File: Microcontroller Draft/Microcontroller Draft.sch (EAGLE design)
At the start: 18 parts, among them IC1 74LS251N, IC2 PIC16F628P

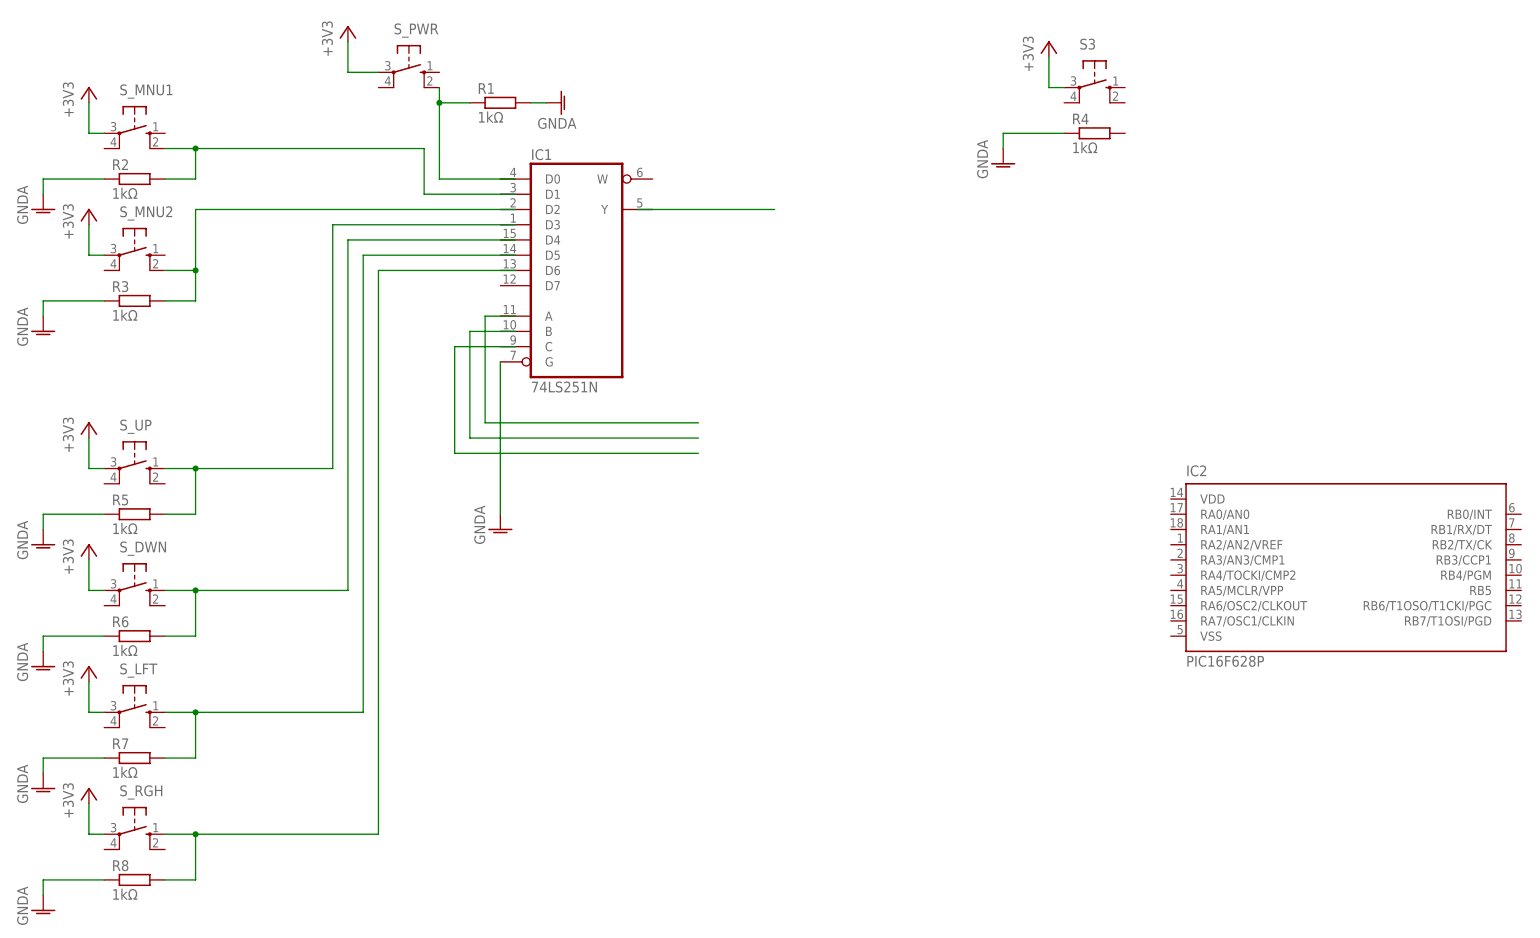
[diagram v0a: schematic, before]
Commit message: Added the Output Logic schematic
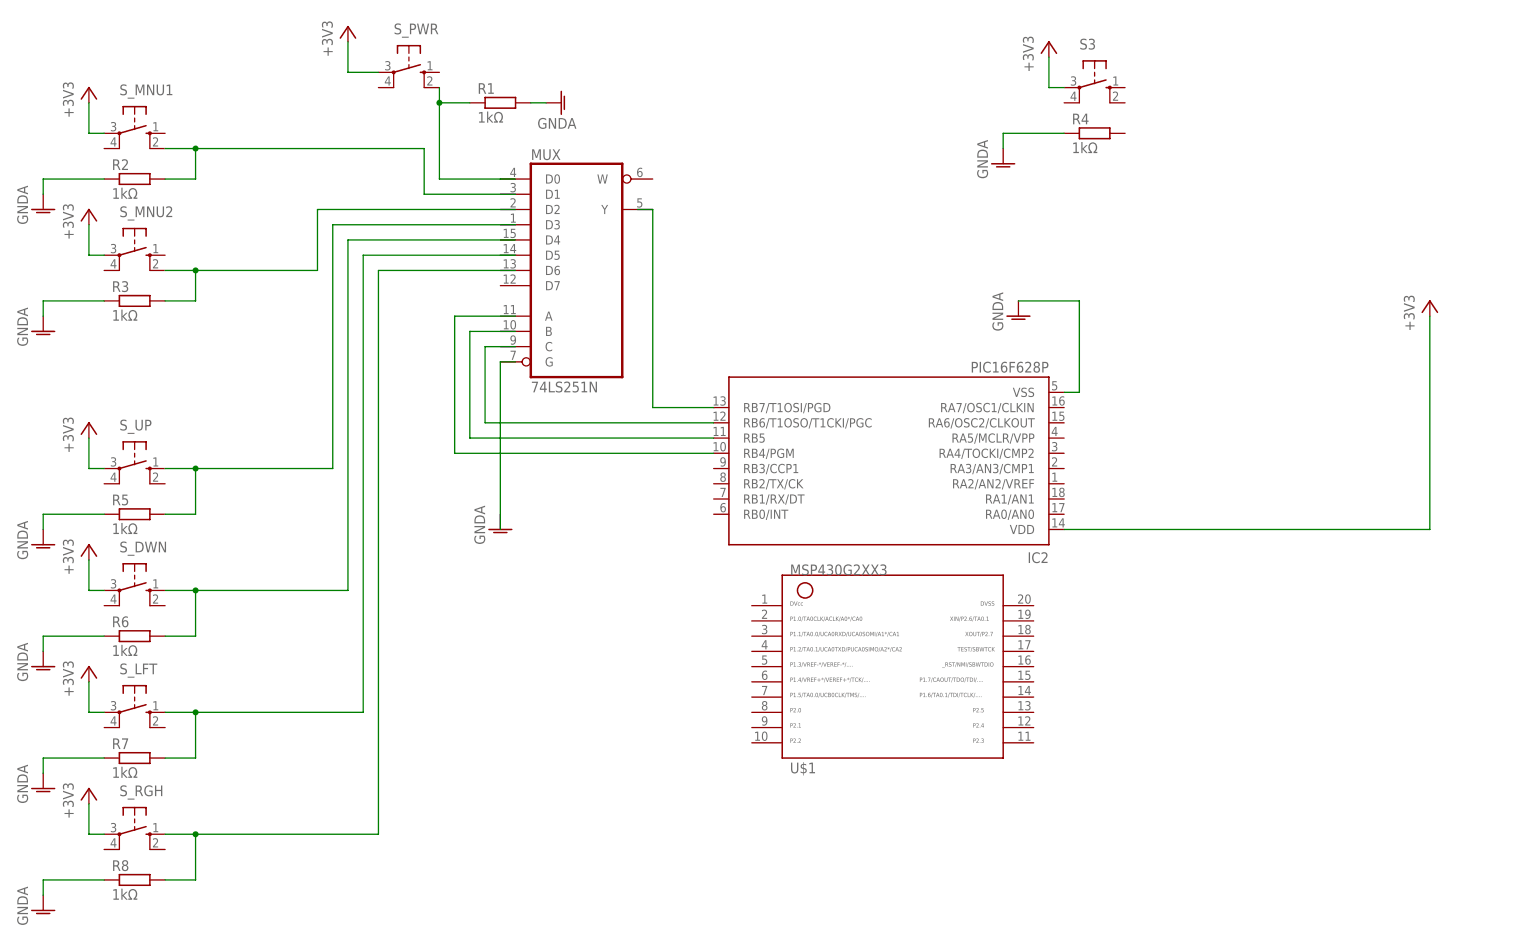
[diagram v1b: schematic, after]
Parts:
- added U$1: G2XX3---N20, TI_MSP430_v16:G2XX3---N20
- renumbered IC1 to MUX
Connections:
- new net N$10: IC2.RB5
- new net N$13: IC2.RB4/PGM
- new net N$4: IC2.RB7/T1OSI/PGD
- new net N$9: IC2.RB6/T1OSO/T1CKI/PGC
- net +3V3: now also IC2.VDD
- net GNDA: now also IC2.VSS; no longer MUXA.G
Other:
- moved on the sheet: IC2
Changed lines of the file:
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@@
 <layer number="48" name="Document" color="7" fill="1" visible="no" active="no"/>
 <layer number="49" name="Reference" color="7" fill="1" visible="no" active="no"/>
+<layer number="50" name="dxf" color="7" fill="1" visible="no" active="no"/>
 <layer number="51" name="tDocu" color="6" fill="1" visible="no" active="no"/>
 <layer number="52" name="bDocu" color="7" fill="1" visible="no" active="no"/>
@@
 <layer number="97" name="Info" color="7" fill="1" visible="yes" active="yes"/>
 <layer number="98" name="Guide" color="6" fill="1" visible="yes" active="yes"/>
+<layer number="100" name="Muster" color="7" fill="1" visible="yes" active="yes"/>
+<layer number="101" name="Flex-Kleb" color="1" fill="7" visible="yes" active="yes"/>
+<layer number="102" name="fp2" color="7" fill="1" visible="yes" active="yes"/>
+<layer number="103" name="fp3" color="7" fill="1" visible="yes" active="yes"/>
+<layer number="104" name="fp4" color="7" fill="1" visible="yes" active="yes"/>
+<layer number="105" name="Beschreib" color="9" fill="1" visible="yes" active="yes"/>
+<layer number="106" name="BGA-Top" color="4" fill="1" visible="yes" active="yes"/>
+<layer number="107" name="BD-Top" color="5" fill="1" visible="yes" active="yes"/>
+<layer number="108" name="fp8" color="7" fill="1" visible="yes" active="yes"/>
+<layer number="109" name="fp9" color="7" fill="1" visible="yes" active="yes"/>
+<layer number="110" name="fp0" color="7" fill="1" visible="yes" active="yes"/>
+<layer number="116" name="Patch_BOT" color="9" fill="4" visible="yes" active="yes"/>
+<layer number="121" name="tTestdril" color="7" fill="1" visible="yes" active="yes"/>
+<layer number="122" name="bTestdril" color="7" fill="1" visible="yes" active="yes"/>
+<layer number="123" name="tTestmark" color="7" fill="1" visible="yes" active="yes"/>
+<layer number="124" name="bTestmark" color="7" fill="1" visible="yes" active="yes"/>
+<layer number="131" name="tAdjust" color="7" fill="1" visible="yes" active="yes"/>
+<layer number="132" name="bAdjust" color="7" fill="1" visible="yes" active="yes"/>
+<layer number="200" name="200bmp" color="7" fill="1" visible="yes" active="yes"/>
+<layer number="201" name="201bmp" color="7" fill="1" visible="yes" active="yes"/>
+<layer number="202" name="202bmp" color="7" fill="1" visible="yes" active="yes"/>
+<layer number="203" name="203bmp" color="7" fill="1" visible="yes" active="yes"/>
+<layer number="204" name="204bmp" color="7" fill="1" visible="yes" active="yes"/>
+<layer number="205" name="205bmp" color="7" fill="1" visible="yes" active="yes"/>
+<layer number="206" name="206bmp" color="7" fill="1" visible="yes" active="yes"/>
+<layer number="207" name="207bmp" color="7" fill="1" visible="yes" active="yes"/>
+<layer number="208" name="208bmp" color="7" fill="1" visible="yes" active="yes"/>
+<layer number="209" name="209bmp" color="7" fill="1" visible="yes" active="yes"/>
+<layer number="210" name="210bmp" color="7" fill="1" visible="yes" active="yes"/>
+<layer number="250" name="Descript" color="3" fill="1" visible="no" active="no"/>
+<layer number="251" name="SMDround" color="12" fill="11" visible="no" active="no"/>
+<layer number="254" name="OrgLBR" color="7" fill="1" visible="yes" active="yes"/>
 </layers>
 <schematic xreflabel="%F%N/%S.%C%R" xrefpart="/%S.%C%R">
@@
 </classes>
 <parts>
-<part name="IC1" library="74xx-us" deviceset="74*251" device="N" technology="LS"/>
+<part name="MUX" library="74xx-us" deviceset="74*251" device="N" technology="LS"/>
 <part name="IC2" library="microchip" deviceset="PIC16F62*" device="P" technology="8"/>
 <part name="S_PWR" library="switch-omron" deviceset="10-XX" device=""/>
@@
 <part name="+3V8" library="supply1" deviceset="+3V3" device=""/>
 <part name="GND9" library="supply1" deviceset="GNDA" device=""/>
+<part name="GND10" library="supply1" deviceset="GNDA" device=""/>
+<part name="+3V9" library="supply1" deviceset="+3V3" device=""/>
+<part name="U$1" library="TI_MSP430_v16" deviceset="G2XX3---N20" device=""/>
 </parts>
 <sheets>
@@
 </plain>
 <instances>
-<instance part="IC1" gate="A" x="109.22" y="116.84"/>
-<instance part="IC2" gate="G$1" x="236.22" y="68.58"/>
+<instance part="MUX" gate="A" x="109.22" y="116.84"/>
+<instance part="IC2" gate="G$1" x="162.56" y="83.82" rot="R180"/>
 <instance part="S_PWR" gate="1" x="81.28" y="149.86" rot="R270"/>
 <instance part="S_MNU1" gate="1" x="35.56" y="139.7" rot="R270"/>
@@
 <instance part="+3V8" gate="G$1" x="27.94" y="30.48"/>
 <instance part="GND9" gate="1" x="96.52" y="73.66"/>
+<instance part="GND10" gate="1" x="182.88" y="109.22"/>
+<instance part="+3V9" gate="G$1" x="251.46" y="111.76"/>
+<instance part="U$1" gate="G$1" x="162.56" y="53.34"/>
 </instances>
 <busses>
@@
 <wire x1="91.44" y1="144.78" x2="86.36" y2="144.78" width="0.1524" layer="91"/>
 <junction x="86.36" y="144.78"/>
-<pinref part="IC1" gate="A" pin="D0"/>
+<pinref part="MUX" gate="A" pin="D0"/>
 </segment>
 </net>
@@
 <wire x1="27.94" y1="22.86" x2="30.48" y2="22.86" width="0.1524" layer="91"/>
 </segment>
+<segment>
+<pinref part="IC2" gate="G$1" pin="VDD"/>
+<wire x1="190.5" y1="73.66" x2="251.46" y2="73.66" width="0.1524" layer="91"/>
+<wire x1="251.46" y1="73.66" x2="251.46" y2="109.22" width="0.1524" layer="91"/>
+<pinref part="+3V9" gate="G$1" pin="+3V3"/>
+</segment>
 </net>
 <net name="GNDA" class="0">
@@
 </segment>
 <segment>
-<pinref part="IC1" gate="A" pin="G"/>
-<wire x1="96.52" y1="101.6" x2="96.52" y2="76.2" width="0.1524" layer="91"/>
-<pinref part="GND9" gate="1" pin="GNDA"/>
+<pinref part="IC2" gate="G$1" pin="VSS"/>
+<wire x1="190.5" y1="96.52" x2="193.04" y2="96.52" width="0.1524" layer="91"/>
+<wire x1="193.04" y1="96.52" x2="193.04" y2="111.76" width="0.1524" layer="91"/>
+<wire x1="193.04" y1="111.76" x2="182.88" y2="111.76" width="0.1524" layer="91"/>
+<pinref part="GND10" gate="1" pin="GNDA"/>
 </segment>
 </net>
@@
 </segment>
 </net>
-<net name="N$4" class="0">
-<segment>
-<pinref part="S_MNU2" gate="1" pin="S1"/>
-<wire x1="40.64" y1="116.84" x2="45.72" y2="116.84" width="0.1524" layer="91"/>
-<wire x1="45.72" y1="111.76" x2="45.72" y2="116.84" width="0.1524" layer="91"/>
-<pinref part="R3" gate="G$1" pin="2"/>
-<wire x1="40.64" y1="111.76" x2="45.72" y2="111.76" width="0.1524" layer="91"/>
-<wire x1="45.72" y1="116.84" x2="45.72" y2="127" width="0.1524" layer="91"/>
-<wire x1="45.72" y1="127" x2="99.06" y2="127" width="0.1524" layer="91"/>
-<junction x="45.72" y="116.84"/>
-</segment>
-</net>
 <net name="N$3" class="0">
 <segment>
@@
 </segment>
 </net>
+<net name="N$11" class="0">
+<segment>
+<pinref part="S_MNU2" gate="1" pin="S1"/>
+<wire x1="40.64" y1="116.84" x2="45.72" y2="116.84" width="0.1524" layer="91"/>
+<wire x1="45.72" y1="111.76" x2="45.72" y2="116.84" width="0.1524" layer="91"/>
+<pinref part="R3" gate="G$1" pin="2"/>
+<wire x1="40.64" y1="111.76" x2="45.72" y2="111.76" width="0.1524" layer="91"/>
+<wire x1="66.04" y1="127" x2="99.06" y2="127" width="0.1524" layer="91"/>
+<wire x1="45.72" y1="116.84" x2="66.04" y2="116.84" width="0.1524" layer="91"/>
+<wire x1="66.04" y1="116.84" x2="66.04" y2="127" width="0.1524" layer="91"/>
+<junction x="45.72" y="116.84"/>
+</segment>
+</net>
 <net name="N$8" class="0">
 <segment>
-<wire x1="99.06" y1="109.22" x2="93.98" y2="109.22" width="0.1524" layer="91"/>
-<wire x1="93.98" y1="109.22" x2="93.98" y2="91.44" width="0.1524" layer="91"/>
-<wire x1="93.98" y1="91.44" x2="129.54" y2="91.44" width="0.1524" layer="91"/>
+<wire x1="99.06" y1="101.6" x2="96.52" y2="101.6" width="0.1524" layer="91"/>
+<wire x1="96.52" y1="101.6" x2="96.52" y2="73.66" width="0.1524" layer="91"/>
 </segment>
 </net>
 <net name="N$9" class="0">
+<segment>
+<wire x1="99.06" y1="104.14" x2="93.98" y2="104.14" width="0.1524" layer="91"/>
+<wire x1="93.98" y1="104.14" x2="93.98" y2="91.44" width="0.1524" layer="91"/>
+<wire x1="93.98" y1="91.44" x2="132.08" y2="91.44" width="0.1524" layer="91"/>
+<pinref part="IC2" gate="G$1" pin="RB6/T1OSO/T1CKI/PGC"/>
+</segment>
+</net>
+<net name="N$10" class="0">
 <segment>
 <wire x1="99.06" y1="106.68" x2="91.44" y2="106.68" width="0.1524" layer="91"/>
 <wire x1="91.44" y1="106.68" x2="91.44" y2="88.9" width="0.1524" layer="91"/>
-<wire x1="91.44" y1="88.9" x2="129.54" y2="88.9" width="0.1524" layer="91"/>
-</segment>
-</net>
-<net name="N$10" class="0">
-<segment>
-<wire x1="99.06" y1="104.14" x2="88.9" y2="104.14" width="0.1524" layer="91"/>
-<wire x1="88.9" y1="104.14" x2="88.9" y2="86.36" width="0.1524" layer="91"/>
-<wire x1="88.9" y1="86.36" x2="129.54" y2="86.36" width="0.1524" layer="91"/>
-</segment>
-</net>
-<net name="N$12" class="0">
-<segment>
-<wire x1="119.38" y1="127" x2="142.24" y2="127" width="0.1524" layer="91"/>
-</segment>
-</net>
+<wire x1="91.44" y1="88.9" x2="132.08" y2="88.9" width="0.1524" layer="91"/>
+<pinref part="IC2" gate="G$1" pin="RB5"/>
+</segment>
+</net>
+<net name="N$13" class="0">
+<segment>
+<wire x1="99.06" y1="109.22" x2="88.9" y2="109.22" width="0.1524" layer="91"/>
+<wire x1="88.9" y1="109.22" x2="88.9" y2="86.36" width="0.1524" layer="91"/>
+<wire x1="88.9" y1="86.36" x2="132.08" y2="86.36" width="0.1524" layer="91"/>
+<pinref part="IC2" gate="G$1" pin="RB4/PGM"/>
+</segment>
+</net>
+<net name="N$4" class="0">
+<segment>
+<wire x1="119.38" y1="127" x2="121.92" y2="127" width="0.1524" layer="91"/>
+<wire x1="121.92" y1="127" x2="121.92" y2="93.98" width="0.1524" layer="91"/>
+<pinref part="IC2" gate="G$1" pin="RB7/T1OSI/PGD"/>
+<wire x1="121.92" y1="93.98" x2="132.08" y2="93.98" width="0.1524" layer="91"/>
+</segment>
+</net>
